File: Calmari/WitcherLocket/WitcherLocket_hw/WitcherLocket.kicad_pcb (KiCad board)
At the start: 2 copper layers, 0 parts

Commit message: witcher locket pcb added
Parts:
- added C1: 0.1u, CAP_0603, F.Cu at (155.0, 107.3)
- added C2: 10u, CAP_0603, F.Cu at (155.1, 110.7)
- added C3: 0.1u, CAP_0603, F.Cu at (155.1, 123.7)
- added C4: 10u, CAP_0603, F.Cu at (155.1, 126.5)
- added D1: BAT54WS, DIODE_SOD323, F.Cu at (157.9, 119.4)
- added D2: LED, LED0603, F.Cu at (181.7, 95.0)
- added D3: LED, LED0603, F.Cu at (186.8, 87.5)
- added D4: LED, LED0603, F.Cu at (181.3, 87.5)
- added D5: LED, LED0603, F.Cu at (176.4, 87.7)
- added D6: LED, LED-3MM, F.Cu at (169.9, 109.0)
- added D7: LED, LED-3MM, F.Cu at (140.1, 109.0)
- added D8: LED, LED-3MM, F.Cu at (140.1, 138.8)
- added D9: LED, LED-3MM, F.Cu at (169.9, 139.1)
- added DA1: NCP1400, SOT23-5, F.Cu at (153.0, 119.7)
- added L1: 22uH, IND_1210, F.Cu at (155.0, 114.5)
- added R1: 47R, RES_0603, F.Cu at (181.5, 91.0)
- added R2: 47R, RES_0603, F.Cu at (144.6, 111.8)
- added R3: 47R, RES_0603, F.Cu at (176.4, 91.3)
- added R4: 47R, RES_0603, F.Cu at (176.6, 94.7)
- added SW1: SWITCH_2X, BUTTON_PSM6, F.Cu at (169.4, 115.7)
- added SW2: SWITCH_2X, BUTTON_PSM6, F.Cu at (140.0, 117.0)
- added SW3: SWITCH_2X, BUTTON_PSM6, F.Cu at (140.3, 131.6)
- added SW4: SWITCH_2X, BUTTON_PSM6, F.Cu at (169.4, 131.6)
- added XL1: CONN_1, SIL1_SQUARE_1MM5, F.Cu at (154.9, 102.4)
- added XL2: CONN_1, SIL1_ROUND_1MM5, F.Cu at (156.3, 145.3)
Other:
- board outline added: 50 x 50 mm

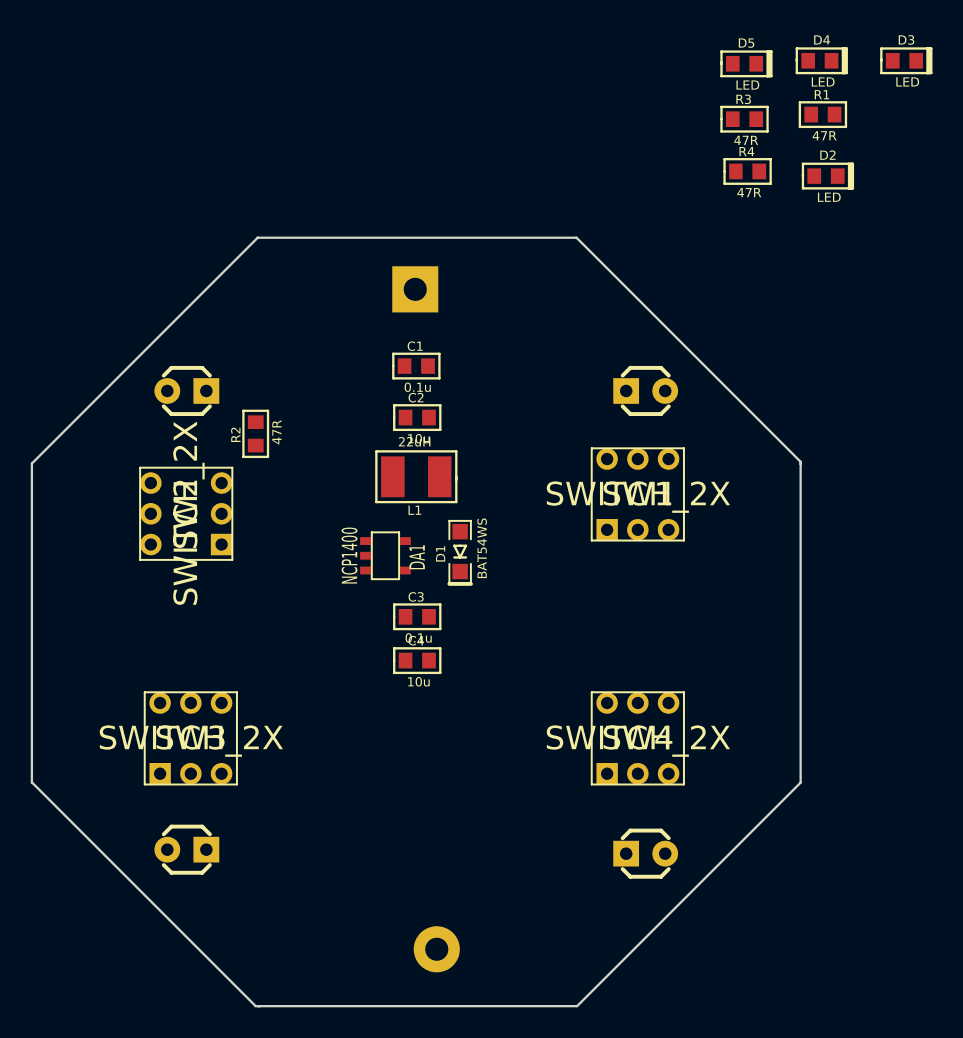
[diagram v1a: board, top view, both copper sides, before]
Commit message: 
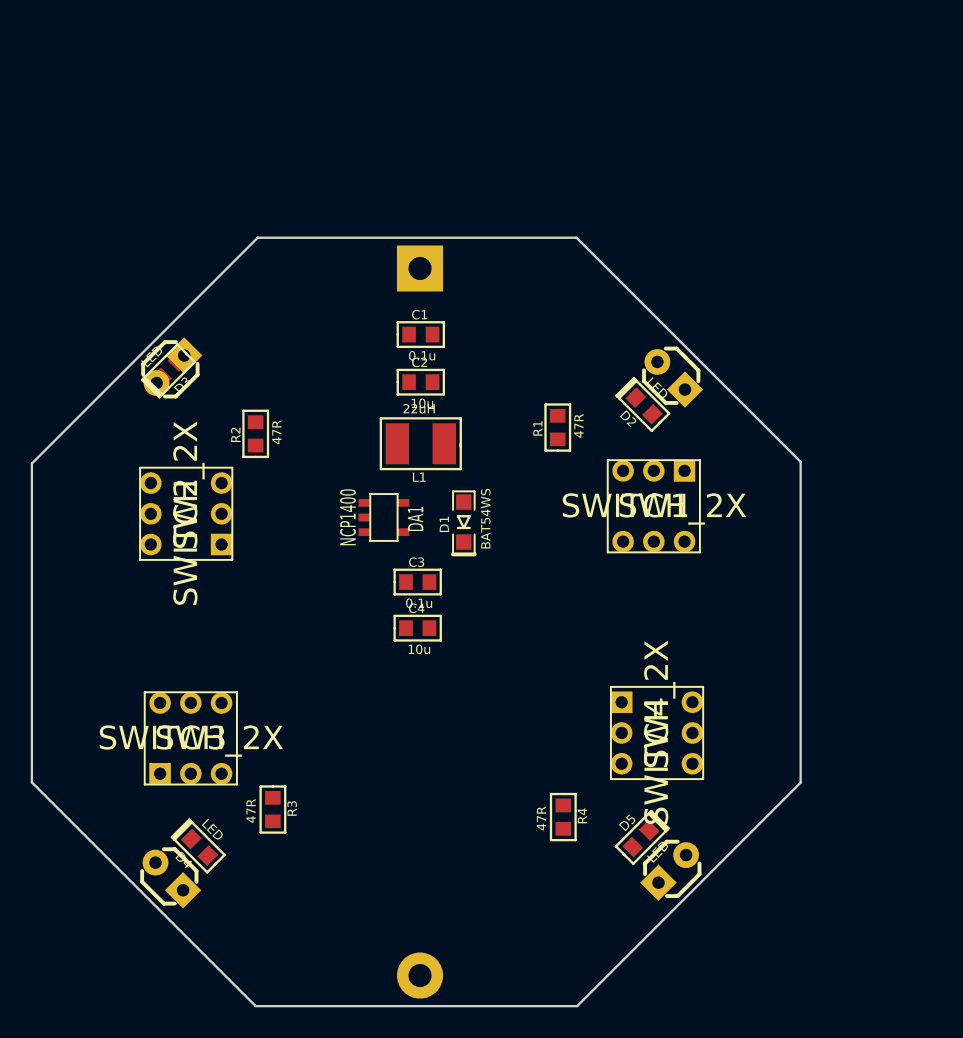
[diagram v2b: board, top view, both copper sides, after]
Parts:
- moved D4 65.2 mm to (140.9, 138.7), turned to 135 degrees
- moved R3 54.4 mm to (145.7, 136.2), turned to 270 degrees
- moved D3 51.8 mm to (139.0, 107.6), turned to 225 degrees
- moved D5 50.9 mm to (169.6, 138.1), turned to 45 degrees
- moved R4 43.7 mm to (164.6, 136.7), turned to 270 degrees
- moved R1 26.7 mm to (164.2, 111.3), turned to 90 degrees
- moved D2 19.1 mm to (169.8, 109.9), turned to 135 degrees
- moved DA1 2.49 mm to (152.9, 117.2)
- moved C2 2.31 mm to (155.3, 108.4)
- moved C3 2.26 mm to (155.1, 121.4)
- moved L1 2.17 mm to (155.3, 112.4)
- moved C4 2.11 mm to (155.1, 124.4)
- moved D8 2.08 mm to (138.9, 140.6), turned to 135 degrees
- moved C1 2.07 mm to (155.3, 105.3)
- moved XL2 2.03 mm to (155.2, 147.0)
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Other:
- outline, holes or cut-outs redrawn

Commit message: 
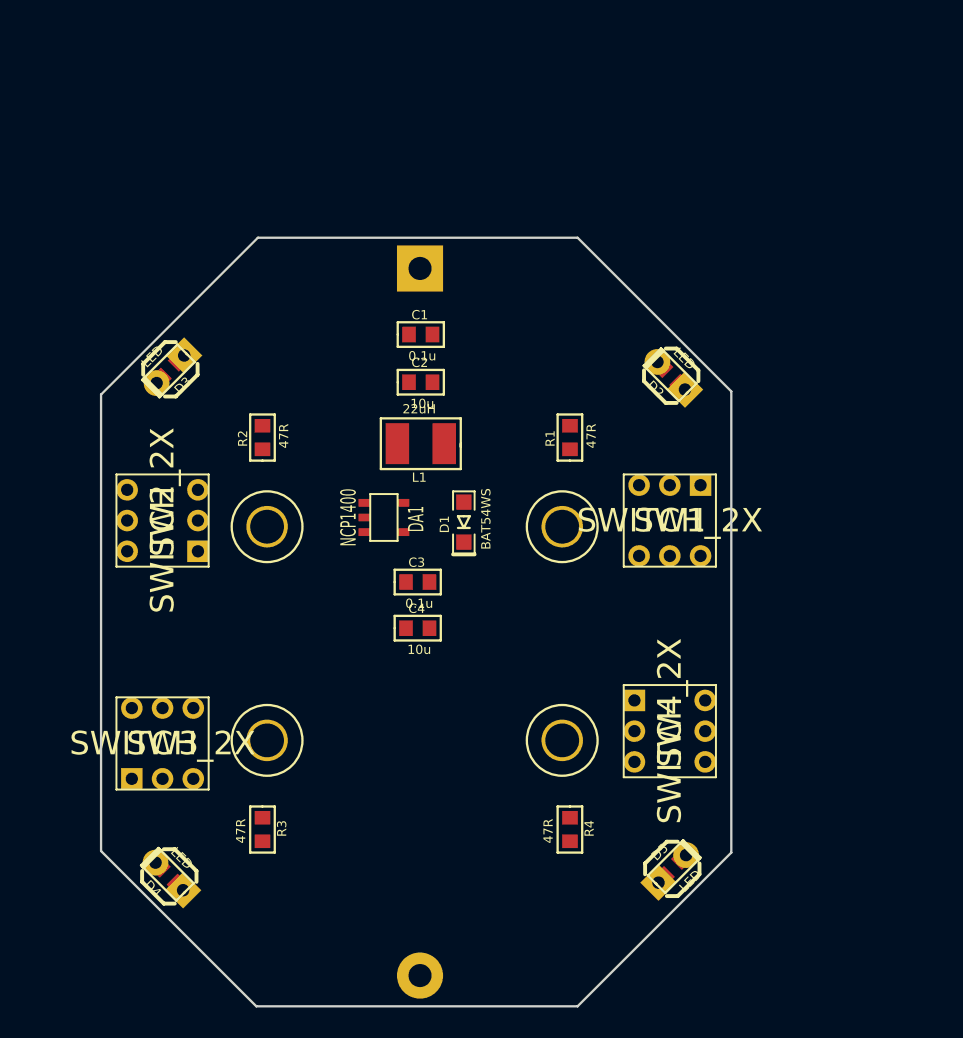
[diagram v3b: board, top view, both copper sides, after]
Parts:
- added HOLE1: HOLE_METALLED, Hole2_2mm, F.Cu at (164.5, 131.7)
- added HOLE2: HOLE_METALLED, Hole2_2mm, F.Cu at (145.3, 131.7)
- added HOLE3: HOLE_METALLED, Hole2_2mm, F.Cu at (164.5, 117.8)
- added HOLE4: HOLE_METALLED, Hole2_2mm, F.Cu at (145.3, 117.8)
- moved D5 2.82 mm to (171.7, 140.0)
- moved D4 2.73 mm to (138.9, 140.5)
- moved D2 2.63 mm to (171.6, 108.0)
- moved SW3 1.87 mm to (138.5, 131.9)
- moved SW2 1.60 mm to (138.5, 117.4)
- moved R3 1.47 mm to (145.0, 137.5)
- moved SW1 1.40 mm to (171.5, 117.4)
- moved R1 1.02 mm to (165.0, 112.0)
- moved R4 0.92 mm to (165.0, 137.5)
- moved SW4 0.84 mm to (171.5, 131.1)
- moved R2 0.50 mm to (145.0, 112.0)
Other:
- board size 50 x 50 mm -> 41 x 50 mm

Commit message: 
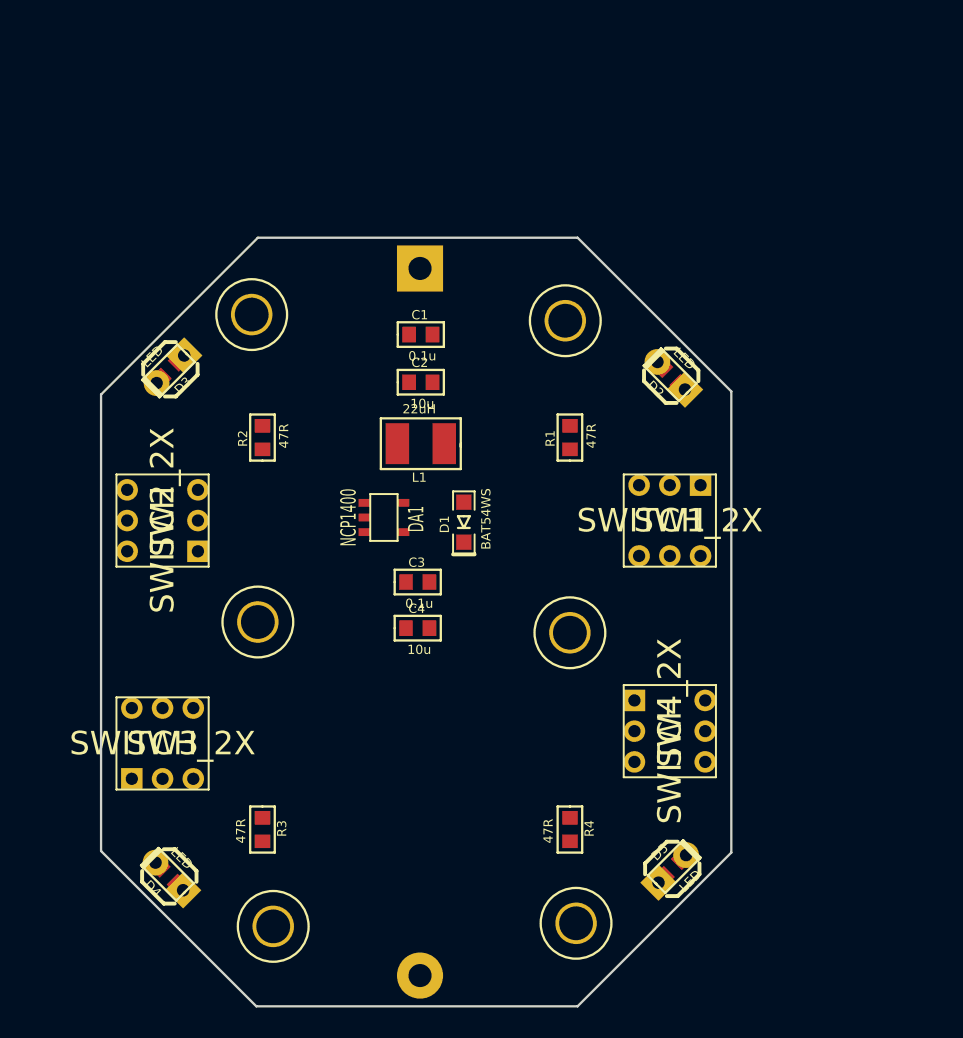
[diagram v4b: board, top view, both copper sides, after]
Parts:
- added HOLE5: HOLE_METALLED, Hole2_2mm, F.Cu at (145.7, 143.8)
- added HOLE6: HOLE_METALLED, Hole2_2mm, F.Cu at (165.4, 143.6)
- moved HOLE4 13.8 mm to (144.3, 104.0)
- moved HOLE3 13.4 mm to (164.7, 104.4)
- moved HOLE2 7.72 mm to (144.7, 124.0)
- moved HOLE1 7.02 mm to (165.0, 124.7)
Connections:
- HOLE1 pad Hle: GND -> (no net)
- HOLE2 pad Hle: GND -> (no net)
- HOLE3 pad Hle: GND -> (no net)
- HOLE4 pad Hle: GND -> (no net)
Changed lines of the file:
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@@
 (kicad_pcb (version 3) (host pcbnew "(2013-03-19 BZR 4004)-stable")
   (general
-    (links 49)
-    (no_connects 41)
-    (area 129.924999 98.924999 180.085001 149.065001)
+    (links 45)
+    (no_connects 37)
+    (area 134.424999 98.924999 175.575001 149.075001)
     (thickness 1.6)
     (drawings 13)
     (tracks 0)
     (zones 0)
-    (modules 29)
+    (modules 31)
     (nets 14)
   )
@@
   (net 4 /PWR_IN)
   (net 5 GND)
-  (net 6 N-000001)
-  (net 7 N-0000010)
-  (net 8 N-0000011)
-  (net 9 N-0000012)
-  (net 10 N-0000016)
-  (net 11 N-0000017)
-  (net 12 N-0000018)
-  (net 13 N-000002)
+  (net 6 N-0000010)
+  (net 7 N-0000011)
+  (net 8 N-0000012)
+  (net 9 N-0000013)
+  (net 10 N-000002)
+  (net 11 N-0000022)
+  (net 12 N-0000024)
+  (net 13 N-000007)
   (net_class Default "This is the default net class."
     (clearance 0.254)
@@
     (add_net /PWR_IN)
     (add_net GND)
-    (add_net N-000001)
     (add_net N-0000010)
     (add_net N-0000011)
     (add_net N-0000012)
-    (add_net N-0000016)
-    (add_net N-0000017)
-    (add_net N-0000018)
+    (add_net N-0000013)
     (add_net N-000002)
+    (add_net N-0000022)
+    (add_net N-0000024)
+    (add_net N-000007)
   )
   (module SOT23-5 (layer F.Cu)
@@
     (pad 1 smd rect (at -0.762 0 270) (size 0.889 1.016)
       (layers F.Cu F.Paste F.Mask)
-      (net 6 N-000001)
+      (net 13 N-000007)
     )
     (pad 2 smd rect (at 0.762 0 270) (size 0.889 1.016)
       (layers F.Cu F.Paste F.Mask)
-      (net 12 N-0000018)
+      (net 8 N-0000012)
     )
     (model 3d\r_0603.wrl
@@
     (pad 1 smd rect (at -0.762 0 270) (size 0.889 1.016)
       (layers F.Cu F.Paste F.Mask)
-      (net 7 N-0000010)
+      (net 6 N-0000010)
     )
     (pad 2 smd rect (at 0.762 0 270) (size 0.889 1.016)
       (layers F.Cu F.Paste F.Mask)
-      (net 9 N-0000012)
+      (net 9 N-0000013)
     )
     (model 3d\r_0603.wrl
@@
     (pad 1 smd rect (at -0.762 0 90) (size 0.889 1.016)
       (layers F.Cu F.Paste F.Mask)
-      (net 13 N-000002)
+      (net 10 N-000002)
     )
     (pad 2 smd rect (at 0.762 0 90) (size 0.889 1.016)
       (layers F.Cu F.Paste F.Mask)
-      (net 11 N-0000017)
+      (net 12 N-0000024)
     )
     (model 3d\r_0603.wrl
@@
     (pad 1 smd rect (at -0.762 0 90) (size 0.889 1.016)
       (layers F.Cu F.Paste F.Mask)
-      (net 8 N-0000011)
+      (net 7 N-0000011)
     )
     (pad 2 smd rect (at 0.762 0 90) (size 0.889 1.016)
       (layers F.Cu F.Paste F.Mask)
-      (net 10 N-0000016)
+      (net 11 N-0000022)
     )
     (model 3d\r_0603.wrl
@@
     (pad A smd rect (at -0.762 0 135) (size 0.889 1.016)
       (layers F.Cu F.Paste F.Mask)
-      (net 10 N-0000016)
+      (net 11 N-0000022)
     )
     (pad C smd rect (at 0.762 0 135) (size 0.889 1.016)
@@
     (pad A smd rect (at -0.762 0 45) (size 0.889 1.016)
       (layers F.Cu F.Paste F.Mask)
-      (net 9 N-0000012)
+      (net 9 N-0000013)
     )
     (pad C smd rect (at 0.762 0 45) (size 0.889 1.016)
@@
     (pad A smd rect (at -0.762 0 135) (size 0.889 1.016)
       (layers F.Cu F.Paste F.Mask)
-      (net 12 N-0000018)
+      (net 8 N-0000012)
     )
     (pad C smd rect (at 0.762 0 135) (size 0.889 1.016)
@@
     (pad A smd rect (at -0.762 0 225) (size 0.889 1.016)
       (layers F.Cu F.Paste F.Mask)
-      (net 11 N-0000017)
+      (net 12 N-0000024)
     )
     (pad C smd rect (at 0.762 0 225) (size 0.889 1.016)
@@
     (pad A thru_hole rect (at -1.27 0 45) (size 1.6764 1.6764) (drill 0.812799)
       (layers *.Cu *.Mask F.SilkS)
-      (net 9 N-0000012)
+      (net 9 N-0000013)
     )
     (pad C thru_hole circle (at 1.27 0 45) (size 1.6764 1.6764) (drill 0.812799)
@@
     (pad A thru_hole rect (at -1.27 0 135) (size 1.6764 1.6764) (drill 0.812799)
       (layers *.Cu *.Mask F.SilkS)
-      (net 12 N-0000018)
+      (net 8 N-0000012)
     )
     (pad C thru_hole circle (at 1.27 0 135) (size 1.6764 1.6764) (drill 0.812799)
@@
     (pad A thru_hole rect (at -1.27 0 225) (size 1.6764 1.6764) (drill 0.812799)
       (layers *.Cu *.Mask F.SilkS)
-      (net 11 N-0000017)
+      (net 12 N-0000024)
     )
     (pad C thru_hole circle (at 1.27 0 225) (size 1.6764 1.6764) (drill 0.812799)
@@
     (pad A thru_hole rect (at -1.27 0 135) (size 1.6764 1.6764) (drill 0.812799)
       (layers *.Cu *.Mask F.SilkS)
-      (net 10 N-0000016)
+      (net 11 N-0000022)
     )
     (pad C thru_hole circle (at 1.27 0 135) (size 1.6764 1.6764) (drill 0.812799)
@@
     (pad 3 thru_hole circle (at 1.99898 2.30124 90) (size 1.39954 1.39954) (drill 0.8001)
       (layers *.Cu *.Mask F.SilkS)
-      (net 13 N-000002)
+      (net 10 N-000002)
     )
     (pad 4 thru_hole circle (at 1.99898 -2.30124 90) (size 1.39954 1.39954) (drill 0.8001)
@@
     (pad 3 thru_hole circle (at 1.99898 2.30124 270) (size 1.39954 1.39954) (drill 0.8001)
       (layers *.Cu *.Mask F.SilkS)
-      (net 7 N-0000010)
+      (net 6 N-0000010)
     )
     (pad 4 thru_hole circle (at 1.99898 -2.30124 270) (size 1.39954 1.39954) (drill 0.8001)
@@
     (pad 3 thru_hole circle (at 1.99898 2.30124 180) (size 1.39954 1.39954) (drill 0.8001)
       (layers *.Cu *.Mask F.SilkS)
-      (net 8 N-0000011)
+      (net 7 N-0000011)
     )
     (pad 4 thru_hole circle (at 1.99898 -2.30124 180) (size 1.39954 1.39954) (drill 0.8001)
@@
     (pad 3 thru_hole circle (at 1.99898 2.30124) (size 1.39954 1.39954) (drill 0.8001)
       (layers *.Cu *.Mask F.SilkS)
-      (net 6 N-000001)
+      (net 13 N-000007)
     )
     (pad 4 thru_hole circle (at 1.99898 -2.30124) (size 1.39954 1.39954) (drill 0.8001)
@@
   )
   (module Hole2_2mm (layer F.Cu)
-    (at 145.3 117.8)
+    (at 144.3 104)
     (fp_text reference HOLE4 (at 0 0.39878) (layer F.SilkS) hide
       (effects (font (size 0.59944 0.59944) (thickness 0.14986)))
@@
     (pad Hle thru_hole circle (at 0 0) (size 2.70002 2.70002) (drill 2.19964)
       (layers *.Cu *.Mask F.SilkS)
-      (net 5 GND)
     )
   )
   (module Hole2_2mm (layer F.Cu)
-    (at 164.5 117.8)
+    (at 164.7 104.4)
     (fp_text reference HOLE3 (at 0 0.39878) (layer F.SilkS) hide
       (effects (font (size 0.59944 0.59944) (thickness 0.14986)))
@@
     (pad Hle thru_hole circle (at 0 0) (size 2.70002 2.70002) (drill 2.19964)
       (layers *.Cu *.Mask F.SilkS)
-      (net 5 GND)
     )
   )
   (module Hole2_2mm (layer F.Cu)
-    (at 145.3 131.7)
+    (at 144.7 124)
     (fp_text reference HOLE2 (at 0 0.39878) (layer F.SilkS) hide
       (effects (font (size 0.59944 0.59944) (thickness 0.14986)))
@@
     (pad Hle thru_hole circle (at 0 0) (size 2.70002 2.70002) (drill 2.19964)
       (layers *.Cu *.Mask F.SilkS)
-      (net 5 GND)
     )
   )
   (module Hole2_2mm (layer F.Cu)
-    (at 164.5 131.7)
+    (at 165 124.7)
     (fp_text reference HOLE1 (at 0 0.39878) (layer F.SilkS) hide
       (effects (font (size 0.59944 0.59944) (thickness 0.14986)))
@@
     (pad Hle thru_hole circle (at 0 0) (size 2.70002 2.70002) (drill 2.19964)
       (layers *.Cu *.Mask F.SilkS)
-      (net 5 GND)
-    )
-  )
+    )
+  )
+  (module Hole2_2mm (layer F.Cu)
+    (at 145.7 143.8)
+    (fp_text reference HOLE5 (at 0 0.39878) (layer F.SilkS) hide
+      (effects (font (size 0.59944 0.59944) (thickness 0.14986)))
+    )
+    (fp_text value HOLE_METALLED (at 0.09906 -0.50038) (layer F.SilkS) hide
+      (effects (font (size 0.59944 0.59944) (thickness 0.14986)))
+    )
+    (fp_circle (center 0 0) (end 2.30124 0) (layer F.SilkS) (width 0.14986))
+    (pad Hle thru_hole circle (at 0 0) (size 2.70002 2.70002) (drill 2.19964)
+      (layers *.Cu *.Mask F.SilkS)
+    )
+  )
+  (module Hole2_2mm (layer F.Cu)
+    (at 165.4 143.6)
+    (fp_text reference HOLE6 (at 0 0.39878) (layer F.SilkS) hide
+      (effects (font (size 0.59944 0.59944) (thickness 0.14986)))
+    )
+    (fp_text value HOLE_METALLED (at 0.09906 -0.50038) (layer F.SilkS) hide
+      (effects (font (size 0.59944 0.59944) (thickness 0.14986)))
+    )
+    (fp_circle (center 0 0) (end 2.30124 0) (layer F.SilkS) (width 0.14986))
+    (pad Hle thru_hole circle (at 0 0) (size 2.70002 2.70002) (drill 2.19964)
+      (layers *.Cu *.Mask F.SilkS)
+    )
+  )
